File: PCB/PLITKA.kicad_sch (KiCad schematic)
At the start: 47 parts, among them SW1 SW_DPDT_x2, SW10 MX_SW_HS, SW11 MX_SW_HS, SW12 MX_SW_HS, SW13 MX_SW_HS, SW14 MX_SW_HS, SW15 MX_SW_HS, SW16 MX_SW_HS, SW17 MX_SW_HS, SW18 MX_SW_HS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

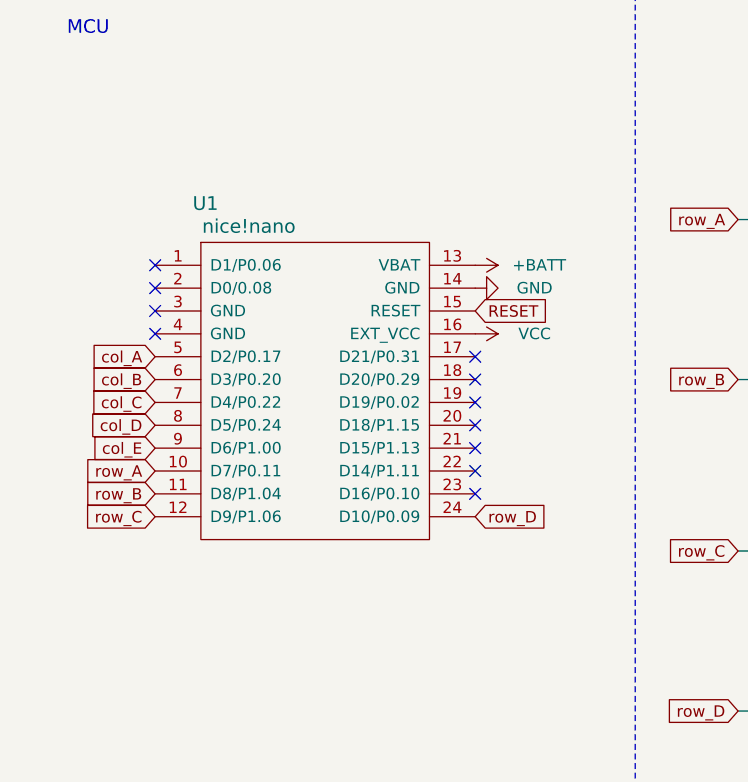
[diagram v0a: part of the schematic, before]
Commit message: Power flags errors correction
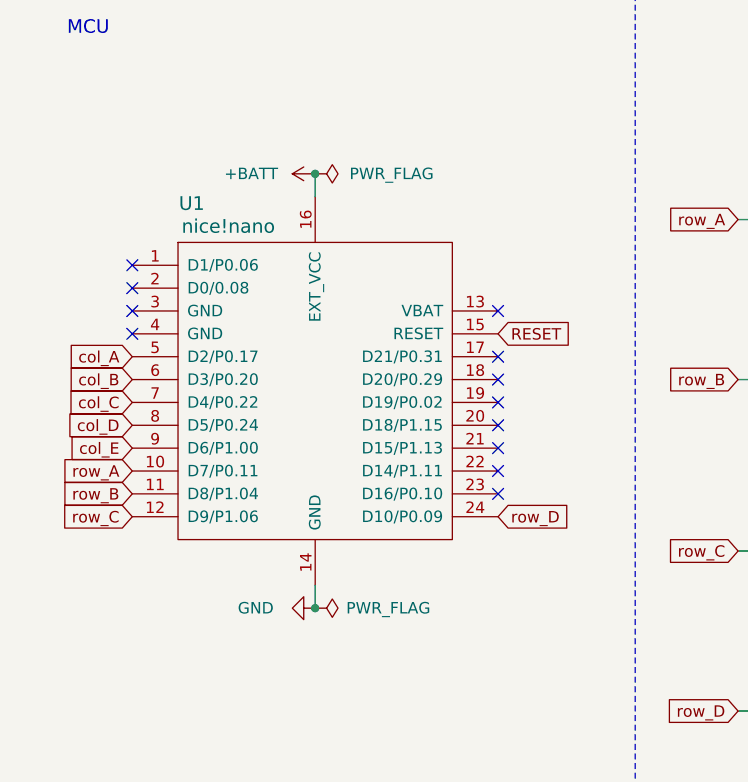
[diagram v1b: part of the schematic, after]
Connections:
- net VCC is gone; now on net +BATT: U1.16 (EXT_VCC)
- net +BATT: no longer U1.13 (VBAT)
- no-connect marks 12 -> 13
